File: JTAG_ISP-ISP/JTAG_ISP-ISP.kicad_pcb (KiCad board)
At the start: 2 copper layers, 23.1 x 46.1 mm, 9 parts, among them J1 Conn_02x03_Odd_Even, J2 Conn_01x08, J3 Conn_01x08

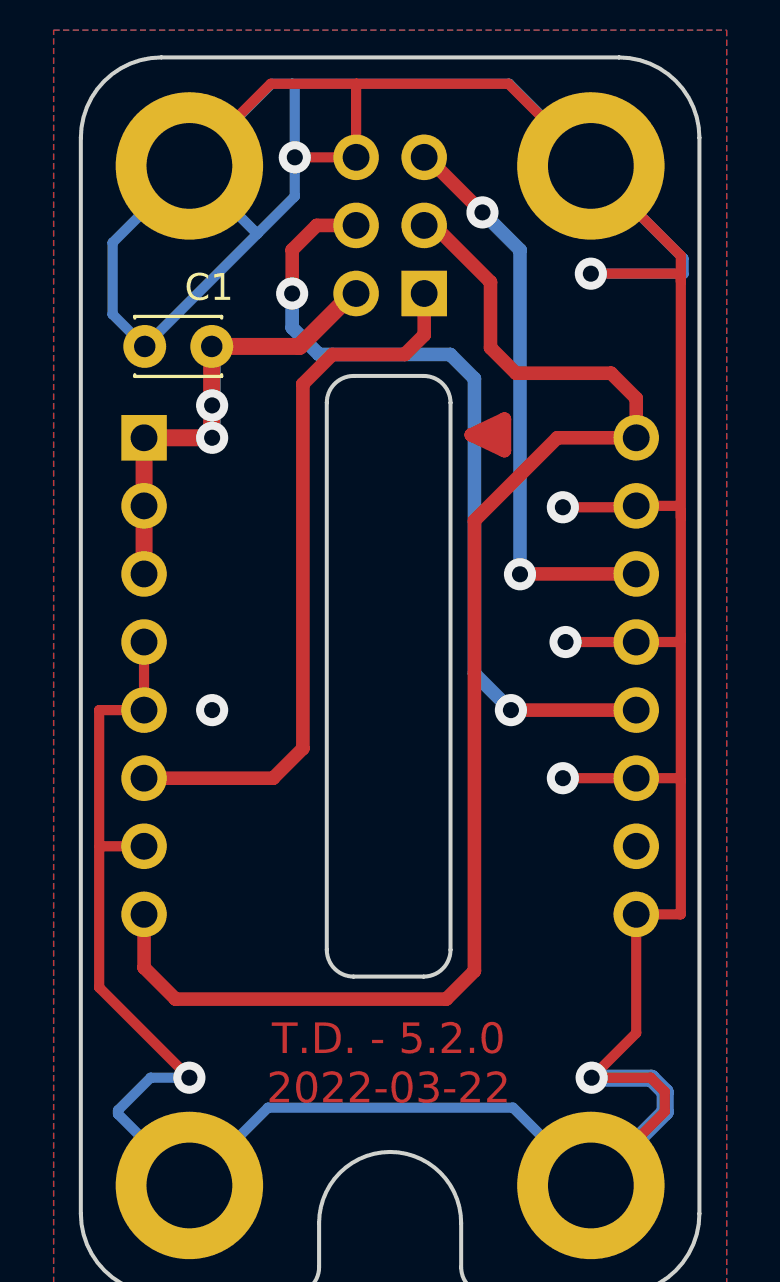
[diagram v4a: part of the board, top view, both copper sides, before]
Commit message: # [PCB] + Ajout de lignes de cote pour le largeur et la hauteur. * Condensateur C1 déplacé sur le dessous du PCB pour ne pas empêcher le PicKit4 de se connecter.     * Modification du routage du ground.     * Modification du routage du Vcc.     - Suppression de vias et de traces maintenant inutiles. * Modification de la position en X du trou pour le PicKit4 afin qu'il soit exactement au centre.     * Actualisation des différents layers en fonction de la nouvelle position ( User.1, User.9, Edge.cuts ). * Vérification de la position en X du header pour le ISP afin qu'il soit exactement au centre. * Mise à jour de la cartouche.     * Date actuelle;     * Version actuelle.
# [SCHÉMA]
* Mise à jour de la cartouche.
    * Date actuelle;
    * Version actuelle.
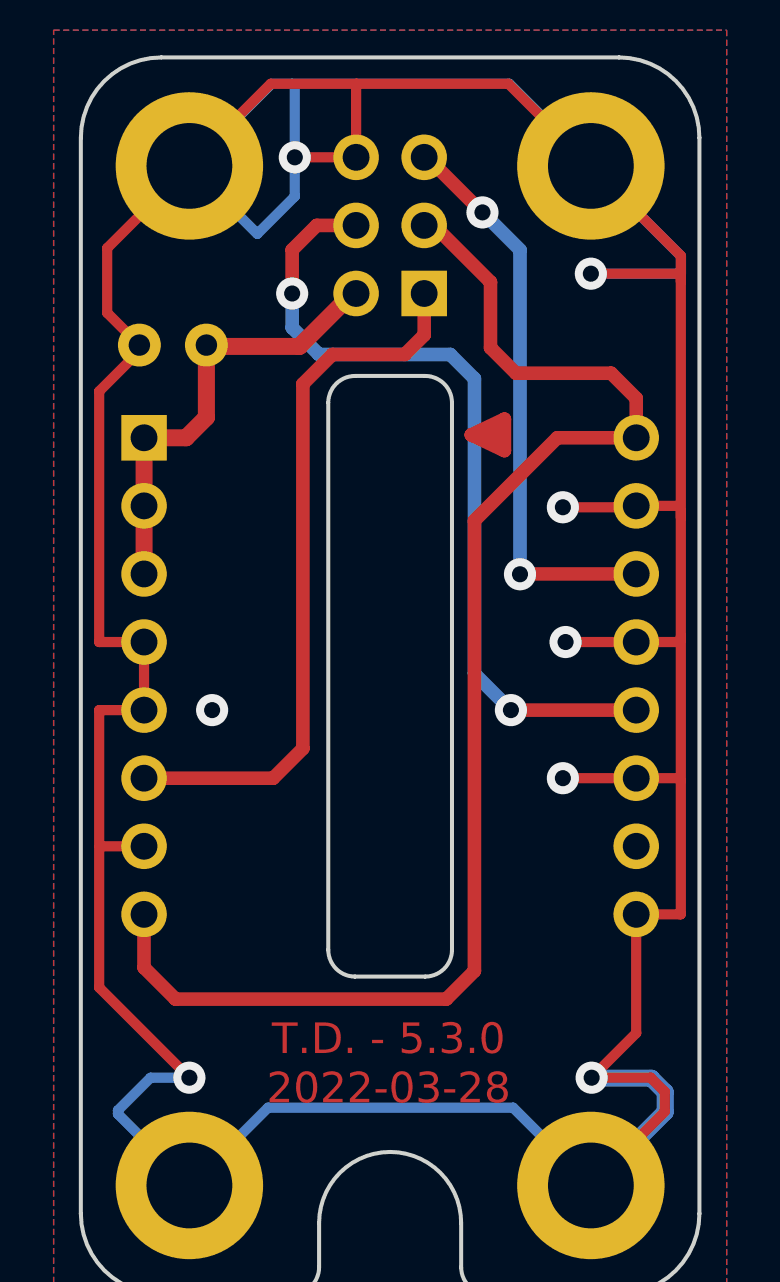
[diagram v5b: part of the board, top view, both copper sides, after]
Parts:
- C1: moved to B.Cu
- moved C1 0.21 mm to (104.6, 56.0)
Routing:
- net GND: track 188.1 -> 195.2 mm
- net +5V: track 20.9 -> 16.7 mm, vias 2 -> 0
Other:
- board text added: "T.D. - 5.3.0 2022-03-28"
- board text removed: "T.D. - 5.2.0 2022-03-22"
